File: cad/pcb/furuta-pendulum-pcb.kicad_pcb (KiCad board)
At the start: 2 copper layers, 132 x 78 mm, 13 parts, among them J1 Pololu Motor+Encoder, J2 AMT103-V, J3 Pololu TB9051FTG Driver, J4 CT3151SP-0 (BLK), J5 CT3151SP-2 (RED), J6 Conn_01x02, J7 Conn_01x02, SW1 SW_SPDT_312, SW2 SW_SPDT_312, SW3 SW_SPDT_312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

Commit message: add current sensor breakout board
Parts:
- added U3: ~, Library:Pololu ACS724 Current Sensor, F.Cu at (92.0, 101.4)
- J2: footprint Connector_PinHeader_2.54mm:PinHeader_1x04_P2.54mm_Vertical -> Connector_PinSocket_2.54mm:PinSocket_1x04_P2.54mm_Vertical
- J4: value CT3151SP-0 (BLK) -> Screw_Terminal_01x01
- J5: value CT3151SP-2 (RED) -> Screw_Terminal_01x01
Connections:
- J1 pad 1: Net-(J3-OUT2) -> Net-(U3-IP+)
- U1 pad 24: unconnected-(U1-32-Pad24) -> ISENS
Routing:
- net Net-(J3-OUT1): track 26.3 -> 0.00 mm
- net Net-(J3-OUT2): track 22.7 -> 0.00 mm

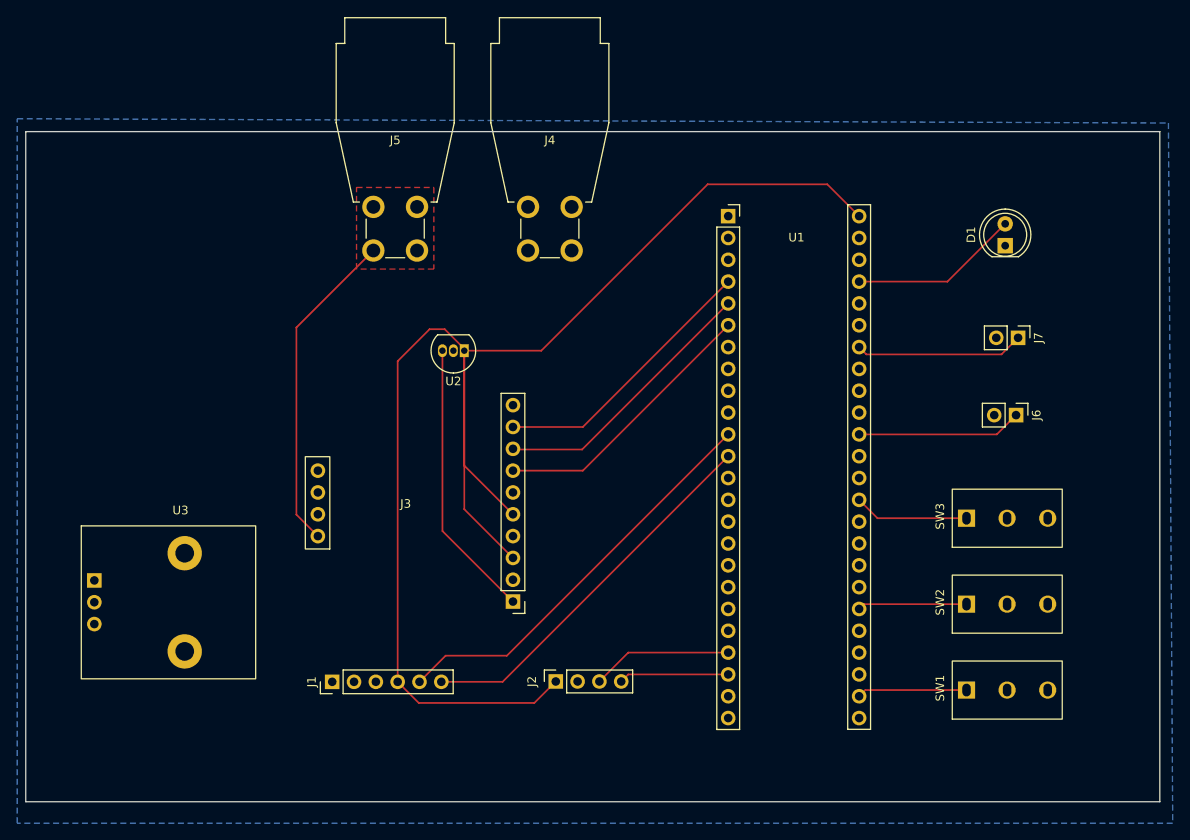
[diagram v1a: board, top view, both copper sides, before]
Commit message: create pcb traces, add mounting holes
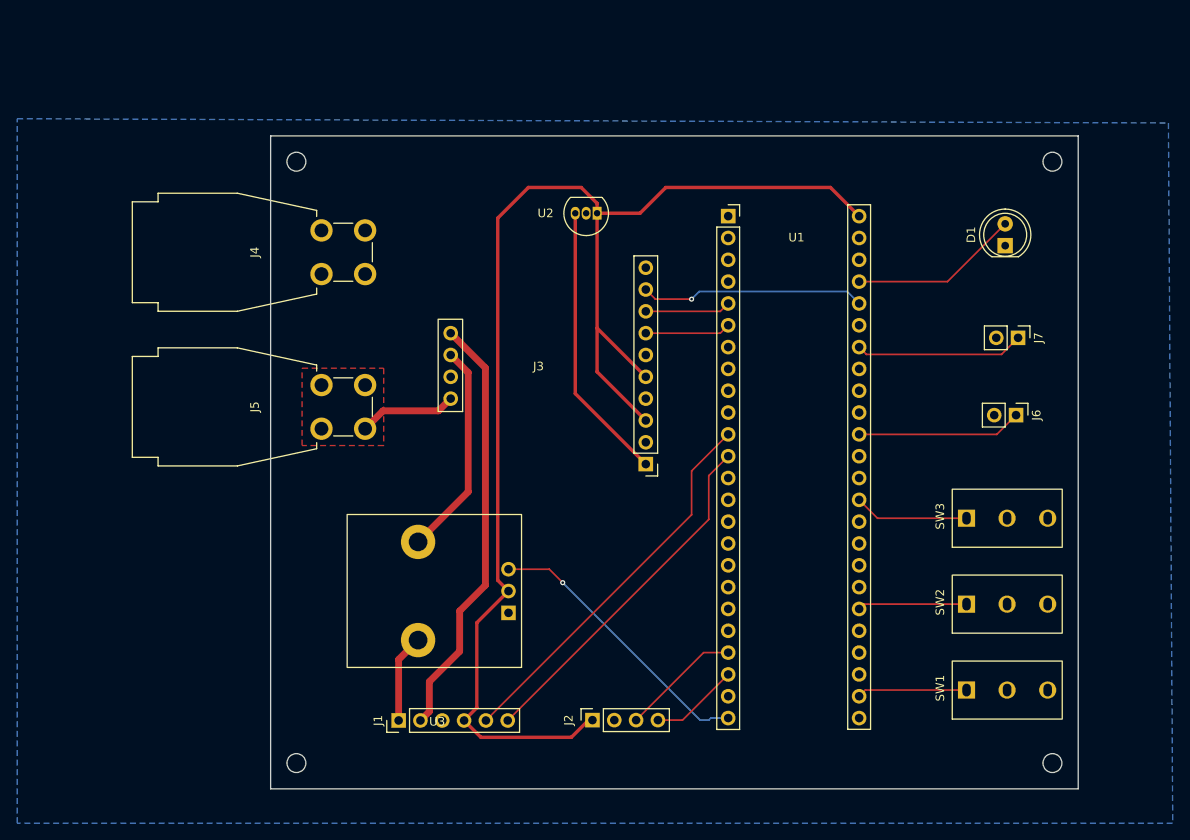
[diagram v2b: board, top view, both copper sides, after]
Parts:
- added H1: MountingHole, MountingHole:MountingHole_2.2mm_M2, F.Cu at (117.0, 59.0)
- added H2: MountingHole, MountingHole:MountingHole_2.2mm_M2, F.Cu at (205.0, 59.0)
- added H3: MountingHole, MountingHole:MountingHole_2.2mm_M2, F.Cu at (205.0, 129.0)
- added H4: MountingHole, MountingHole:MountingHole_2.2mm_M2, F.Cu at (117.0, 129.0)
- moved U3 53.8 mm to (143.2, 117.9), turned to 180 degrees
- moved J4 29.2 mm to (119.9, 67.0), turned to 0 degrees
- moved J5 23.5 mm to (119.9, 85.0), turned to 0 degrees
- moved U2 22.2 mm to (152.0, 65.0)
- moved J3 22.2 mm to (157.7, 94.2)
- moved J1 8.94 mm to (128.9, 124.0)
- moved J2 6.20 mm to (151.5, 124.0)
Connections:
- J1 pad 1: Net-(U3-IP+) -> Net-(U3-IP-)
- U1 pad 4: OCM -> unconnected-(U1-2-Pad4)
- U1 pad 44: unconnected-(U1-22-Pad44) -> OCM
- U3 pad 4: Net-(J3-OUT2) -> Net-(U3-IP-)
- U3 pad 5: Net-(U3-IP+) -> Net-(J3-OUT2)
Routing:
- net Net-(J3-OUT1): track 0.00 -> 49.9 mm
- net ISENS: track 0.00 -> 33.0 mm, vias 0 -> 1
- net +12V: track 38.0 -> 11.4 mm
- net Net-(J3-OUT2): track 0.00 -> 25.0 mm
- net PWM1: track 32.1 -> 9.97 mm
- net PWM2: track 32.1 -> 9.97 mm
- net +5V: track 171.6 -> 160.3 mm
- net Net-(U3-IP-): track 0.00 -> 10.3 mm
- net OCM: track 32.1 -> 26.2 mm, vias 0 -> 1
- net ENC1_A: track 47.9 -> 45.0 mm
- net ENC1_B: track 44.3 -> 41.4 mm
- net ENC2_A: track 12.8 -> 10.4 mm
- net ENC2_B: track 16.4 -> 14.0 mm
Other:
- board size 132 x 78 mm -> 94 x 76 mm
- rule pad_to_mask_clearance: 0 -> 0.0508

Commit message: board updates
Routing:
- net OCM: track 26.2 -> 25.5 mm
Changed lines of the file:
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@@
 	)
 	(segment
-		(start 158.7876 75)
-		(end 163 75)
-		(width 0.2)
-		(layer "F.Cu")
-		(net 11)
-	)
-	(segment
-		(start 157.6676 73.88)
-		(end 158.7876 75)
+		(start 162 74.111)
+		(end 157.8986 74.111)
+		(width 0.2)
+		(layer "F.Cu")
+		(net 11)
+	)
+	(segment
+		(start 157.8986 74.111)
+		(end 157.6676 73.88)
 		(width 0.2)
 		(layer "F.Cu")
@@
 	)
 	(via
-		(at 163 75)
+		(at 162 74.111)
 		(size 0.6)
 		(drill 0.3)
@@
 	)
 	(segment
-		(start 163 75)
-		(end 163.889 74.111)
-		(width 0.2)
-		(layer "B.Cu")
-		(net 11)
-	)
-	(segment
-		(start 163.889 74.111)
-		(end 181.111 74.111)
-		(width 0.2)
-		(layer "B.Cu")
-		(net 11)
-	)
-	(segment
 		(start 181.111 74.111)
 		(end 182.5 75.5)
+		(width 0.2)
+		(layer "B.Cu")
+		(net 11)
+	)
+	(segment
+		(start 162 74.111)
+		(end 181.111 74.111)
 		(width 0.2)
 		(layer "B.Cu")
@@
 	)
 	(segment
-		(start 165.24 123.76)
+		(start 163.76 123.76)
 		(end 167.26 123.76)
 		(width 0.2)
@@
 	(segment
 		(start 148 108)
-		(end 164 124)
-		(width 0.2)
-		(layer "B.Cu")
-		(net 56)
-	)
-	(segment
-		(start 164 124)
-		(end 165 124)
-		(width 0.2)
-		(layer "B.Cu")
-		(net 56)
-	)
-	(segment
-		(start 165 124)
-		(end 165.24 123.76)
-		(width 0.2)
-		(layer "B.Cu")
+		(end 163.76 123.76)
+		(width 0.2)
+		(layer "B.Cu")
